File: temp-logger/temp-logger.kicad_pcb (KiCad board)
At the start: 2 copper layers, 40 x 40 mm, 23 parts, among them J1 USB_OTG, J2 CONN_01X03, SW1 SW_Push, SW2 SW_Push, U1 AP1117-33, U2 ESP-12E, U3 HTU21D

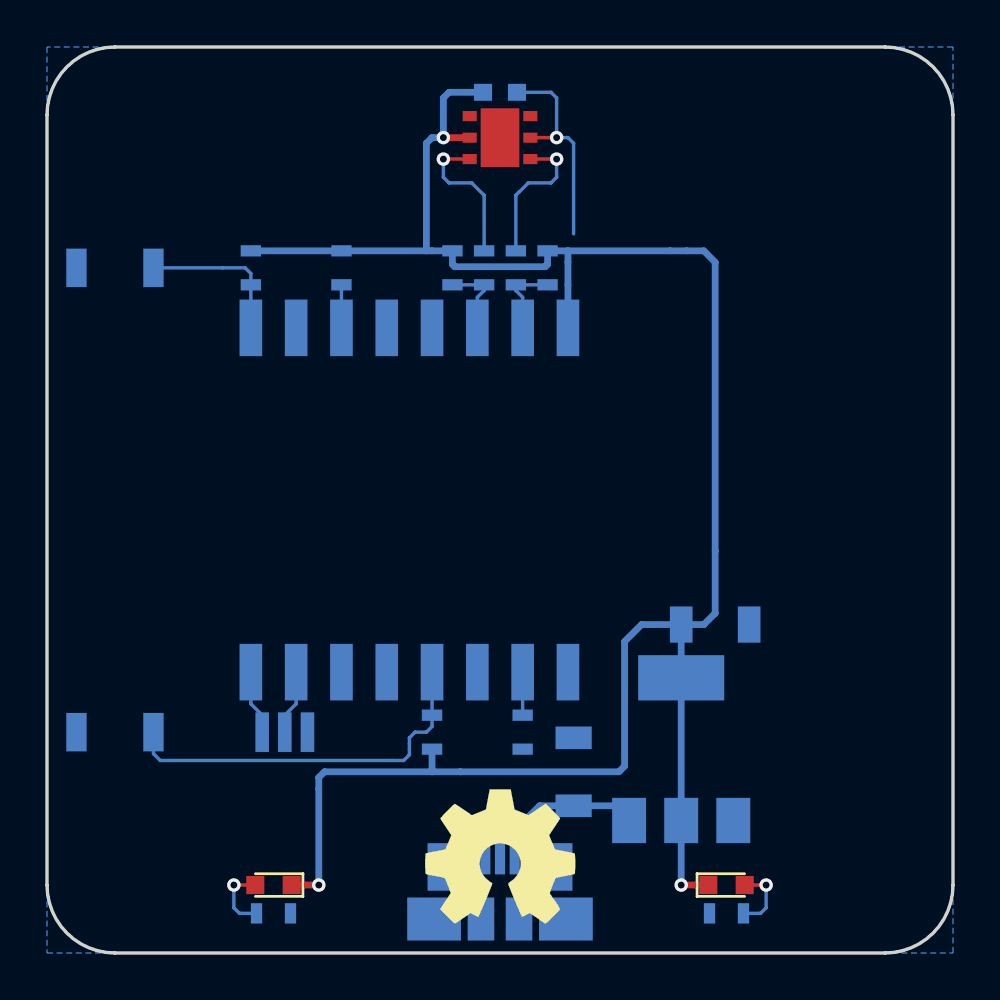
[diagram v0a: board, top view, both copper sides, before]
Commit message: Hooked up LEDs
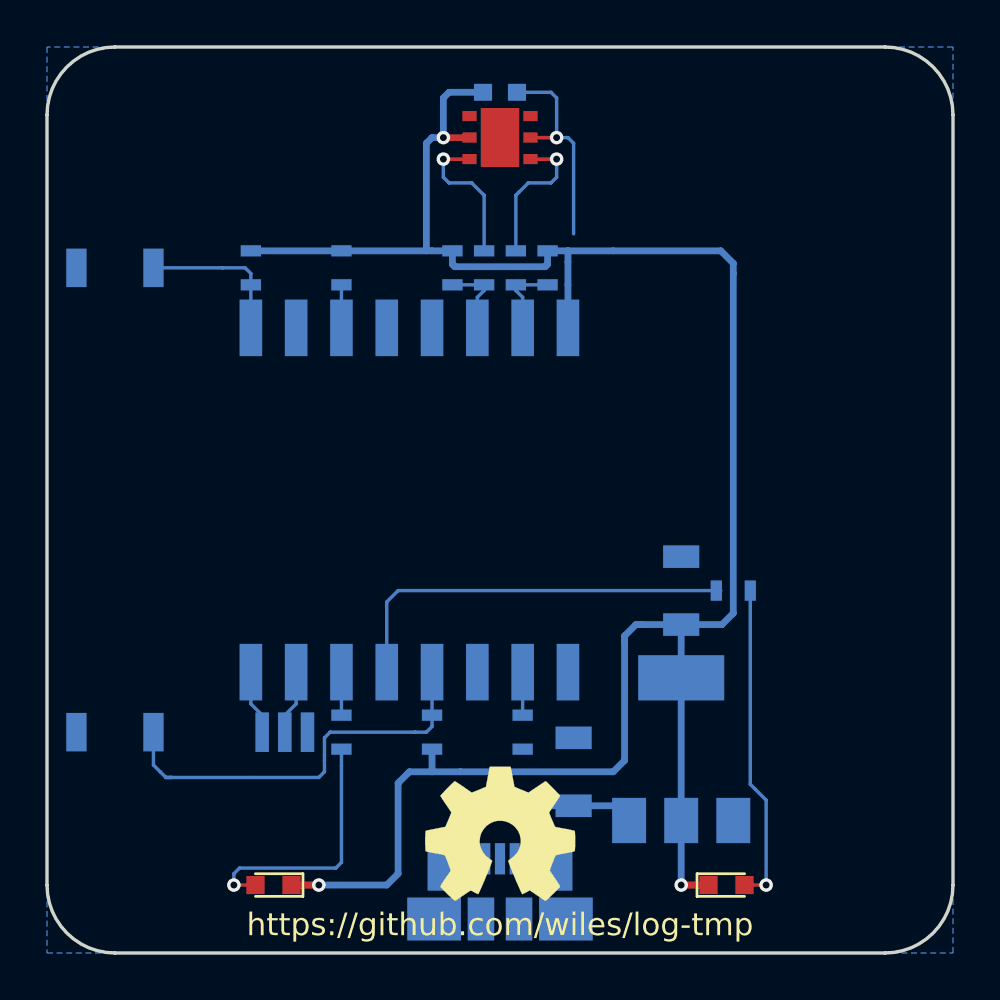
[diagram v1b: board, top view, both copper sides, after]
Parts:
- moved R6 14.3 mm to (110.3, 104.0)
- moved R5 8.54 mm to (93.0, 110.2), turned to 90 degrees
- moved C2 2.12 mm to (108.0, 104.0), turned to 90 degrees
- moved REF*** 1.00 mm to (100.0, 114.8)
- turned J2 to 270 degrees
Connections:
- J2 pad 1: GND -> Net-(J2-Pad1)
- J2 pad 3: Net-(J2-Pad3) -> GND
- U2 pad 19: Net-(U2-Pad19) -> Net-(R6-Pad2)
- U2 pad 20: Net-(U2-Pad20) -> Net-(R5-Pad2)
- U2 pad 22: Net-(J2-Pad3) -> Net-(J2-Pad1)
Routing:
- net Net-(R6-Pad2): track 0.00 -> 18.1 mm
- net Net-(D2-Pad2): track 3.05 -> 14.2 mm
- net Net-(D1-Pad2): track 3.05 -> 11.4 mm
- net Net-(J2-Pad3): track 2.86 -> 0.00 mm
- net Net-(J2-Pad1): track 0.00 -> 2.86 mm
- net Net-(R5-Pad2): track 0.00 -> 1.90 mm
- net Net-(R3-Pad2): track 16.8 -> 18.4 mm
- net +3V3: track 94.3 -> 95.5 mm
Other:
- board text added: "Rev. 1"
- board text added: "https://github.com/wiles/log-tmp"

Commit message: Fixed R6 label location
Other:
- board text added: "Rev. 2"
- board text removed: "Rev. 1"
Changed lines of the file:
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@@
     (tags "resistor 0603")
     (attr smd)
-    (fp_text reference R6 (at 2.25 0 180) (layer B.SilkS)
+    (fp_text reference R6 (at 0 1.4 180) (layer B.SilkS)
       (effects (font (size 1 1) (thickness 0.15)) (justify mirror))
     )
@@
     )
   )
-  (gr_text "Rev. 1" (at 90 118.75) (layer B.SilkS)
+  (gr_text "Rev. 2" (at 90 118.75) (layer B.SilkS)
     (effects (font (size 1 1) (thickness 0.15)) (justify mirror))
   )

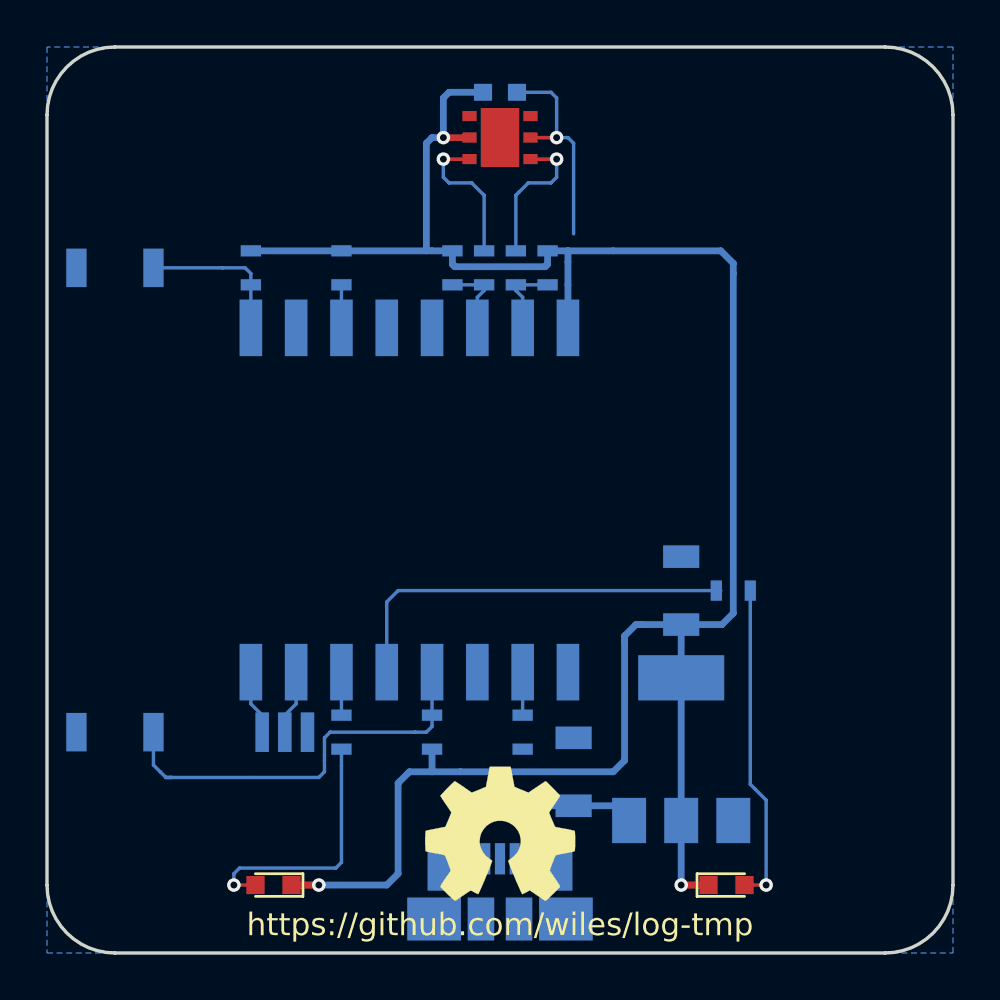
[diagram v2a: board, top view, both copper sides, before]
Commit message: Redid layout to make soldering and programming easier
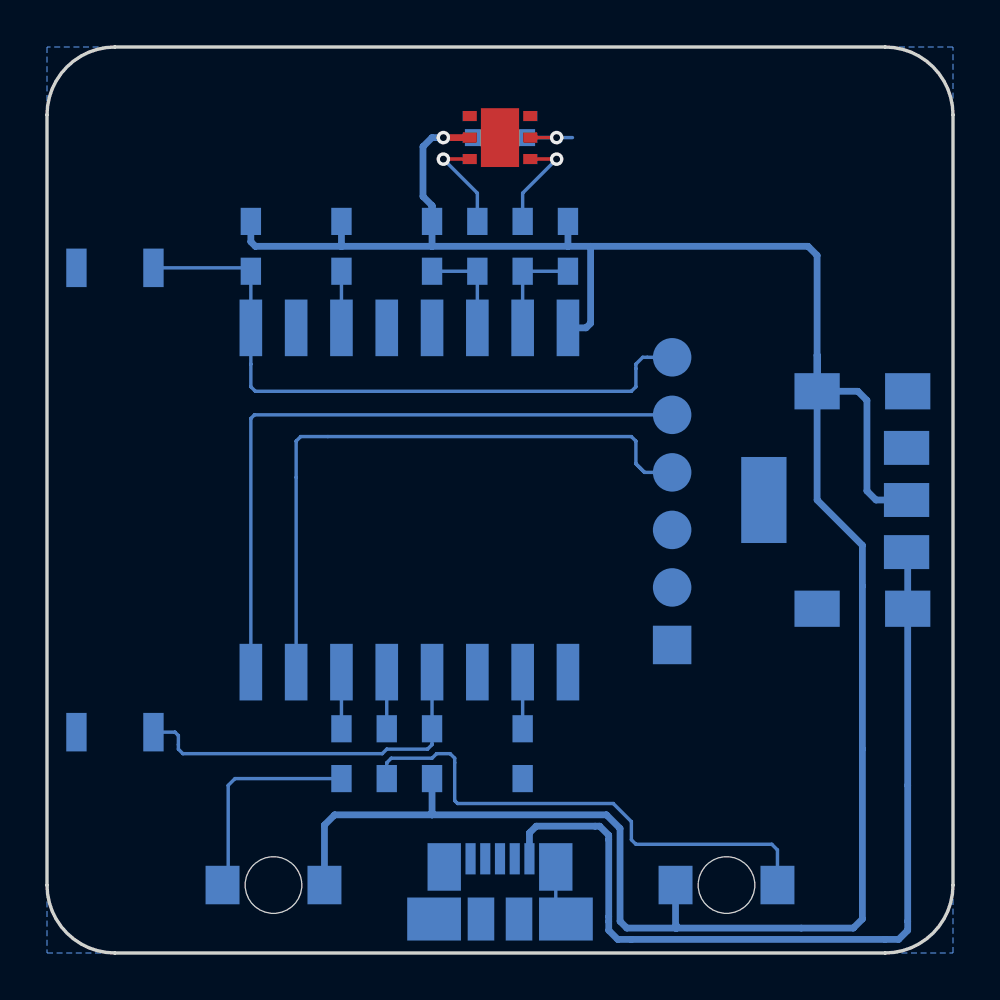
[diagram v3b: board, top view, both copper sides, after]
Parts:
- added REF**: MountingHole_2.5mm, Mounting_Holes:MountingHole_2.5mm, F.Cu at (110.0, 117.0)
- added REF**: MountingHole_2.5mm, Mounting_Holes:MountingHole_2.5mm, F.Cu at (90.0, 117.0)
- C1, C2: footprint Capacitors_SMD:C_1206 -> Capacitors_SMD:C_1206_HandSoldering
- C3: footprint Capacitors_SMD:C_0603 -> Capacitors_SMD:C_0603_HandSoldering
- D1, D2: footprint LEDs:LED_0603 -> LEDs:LED_1206_HandSoldering; moved to B.Cu
- J2: value CONN_01X03 -> FTDI; footprint Pin_Headers:Pin_Header_Straight_1x03_Pitch1.00mm_SMD_Pin1Right -> Pin_Headers:Pin_Header_Straight_1x06_Pitch2.54mm
- JP1, JP2, R1, R2, R3, R4, R5, R6, R7, R8: footprint Resistors_SMD:R_0603 -> Resistors_SMD:R_0603_HandSoldering
- REF***: moved to B.Cu
- SW1: value SW_Push -> RST
- SW2: value SW_Push -> PROG
- U1: footprint TO_SOT_Packages_SMD:SOT-223-3Lead_TabPin2 -> TO_SOT_Packages_SMD:SOT-223
- moved REF*** 29.4 mm to (109.0, 86.8), turned to 180 degrees
- moved J2 17.5 mm to (107.6, 106.4), turned to 0 degrees
- moved R6 16.9 mm to (95.0, 111.2), turned to 90 degrees
- moved C1 14.6 mm to (116.0, 104.8), turned to 180 degrees
- moved U1 12.9 mm to (114.8, 100.0), turned to 180 degrees
- moved C2 11.9 mm to (116.0, 95.2), turned to 0 degrees
- moved C3 2.00 mm to (100.0, 84.0)
- moved R7 1.31 mm to (103.0, 88.8)
- moved R8 1.31 mm to (97.0, 88.8)
- moved JP1 1.00 mm to (101.0, 88.8)
- moved JP2 1.00 mm to (99.0, 88.8)
- moved R1 0.95 mm to (93.0, 88.8)
- moved R2 0.95 mm to (89.0, 88.8)
- moved R3 0.95 mm to (97.0, 111.2)
- moved R4 0.95 mm to (101.0, 111.2)
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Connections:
- J2 pad 1: Net-(J2-Pad1) -> GND
- J2 pad 2: Net-(J2-Pad2) -> (no net)
- J2 pad 3: GND -> (no net)
- R2 pad 2: Net-(R2-Pad2) -> RST
- SW1 pad 2: Net-(R2-Pad2) -> RST
- U2 pad 1: Net-(R2-Pad2) -> RST
- U2 pad 21: Net-(J2-Pad2) -> Net-(J2-Pad4)
- U2 pad 22: Net-(J2-Pad1) -> Net-(J2-Pad5)
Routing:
- net Net-(C1-Pad1): track 7.66 -> 39.4 mm
- net Net-(J2-Pad5): track 0.00 -> 29.9 mm
- net RST: track 0.00 -> 28.8 mm
- net Net-(J2-Pad4): track 0.00 -> 28.7 mm
- net +3V3: track 95.5 -> 117.5 mm, vias 3 -> 1
- net Net-(R6-Pad2): track 18.1 -> 2.30 mm
- net Net-(D2-Pad2): track 14.2 -> 23.0 mm, vias 1 -> 0
- net Net-(R2-Pad2): track 6.80 -> 0.00 mm
- net GND: track 9.62 -> 5.90 mm
- net Net-(J2-Pad2): track 2.86 -> 0.00 mm
- net Net-(J2-Pad1): track 2.86 -> 0.00 mm
- net Net-(R3-Pad2): track 18.4 -> 16.3 mm
- net Net-(D1-Pad2): track 11.4 -> 9.52 mm, vias 1 -> 0
- net Net-(JP2-Pad1): track 6.54 -> 4.73 mm
- net Net-(JP1-Pad2): track 6.54 -> 4.73 mm
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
